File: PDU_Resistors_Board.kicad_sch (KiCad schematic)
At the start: 23 parts

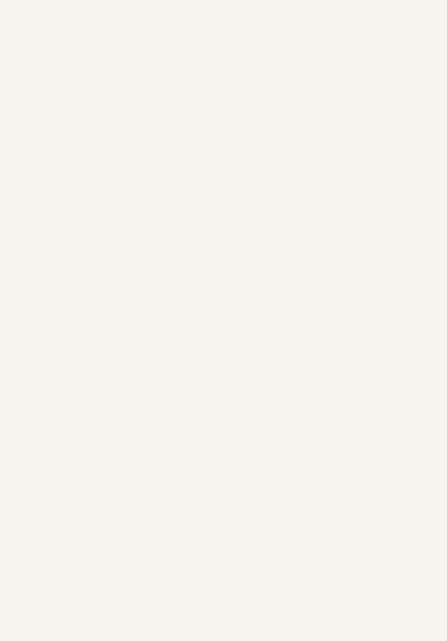
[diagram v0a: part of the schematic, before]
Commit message: VER1.0: исправил Э3
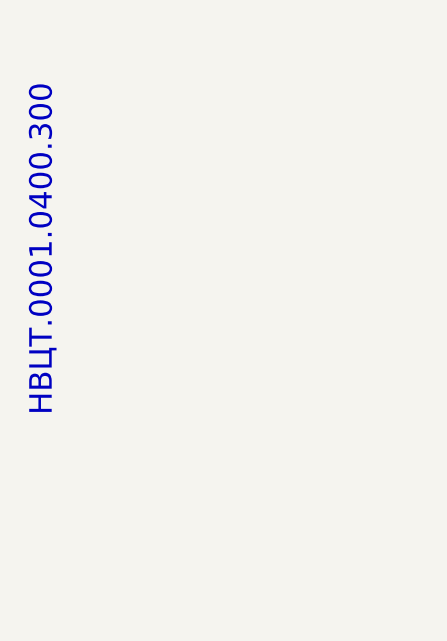
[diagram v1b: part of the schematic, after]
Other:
- note added: "НВЦТ.0001.0400.300"
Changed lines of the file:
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@@
 		(comment 6 "Зубков Д.Н.")
+	)
+	(text "НВЦТ.0001.0400.300"
+		(exclude_from_sim no)
+		(at 16.51 36.068 90)
+		(effects
+			(font
+				(size 2.5 2.5)
+			)
+		)
 	)
 	(text "Схема электрическая принципиальная"

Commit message: VER1.0: исправил Э3
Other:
- note added: "1. Перечень элементов см. НВЦТ.0001.0400.300 ПЭ3."
- note added: "ООО "Электротранспортные"
- note added: "технологии""
- company: ООО "Электротранспортные технологии" -> (none)
- moved on the sheet: H1, H2, H3, H4, J1, J2, J3, R1, R10, R11, R12, R13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
